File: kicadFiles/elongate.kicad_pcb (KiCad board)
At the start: 2 copper layers, 299.3 x 82.3 mm, 123 parts, among them SW1 SW_PUSH, U1 ATMEGA32U4, X1 XTAL_GND

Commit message: [Update] Finished placing components. Almost done routing. Logos still pending.
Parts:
- removed C1, C2, C3, C4, C5, C6, C7: 22pF, Capacitor_SMD:C_0805_2012Metric_Pad1.15x1.40mm_HandSolder
- removed D_0, D_1, D_2, D_3, D_4, D_5, D_6, D_7, D_8, D_9, D_A, D_ALT, D_ALT1, D_B, D_BS, D_C, D_COMMA, D_CTRL, D_CTRL1, D_D, D_DOT, D_DOWN, D_E, D_ENTER, D_F, D_FN1, D_FN2, D_G, D_H, D_I, D_J, D_K, D_L, D_LEFT, D_M, D_N, D_O, D_P, D_Q, D_R, D_RIGHT, D_S, D_SHIFT, D_SPACE, D_T, D_TAB, D_U, D_UP, D_V, D_W, D_WIN, D_X, D_Y, D_Z: D, keyboard_parts:D_SOD123_axial
- removed K_0, K_1, K_2, K_3, K_4, K_5, K_6, K_7, K_8, K_9, K_A, K_ALT1, K_B, K_BS, K_C, K_COMMA, K_D, K_DOT, K_DOWN, K_E, K_F, K_G, K_H, K_I, K_J, K_K, K_L, K_LEFT, K_M, K_N, K_O, K_P, K_Q, K_R, K_RIGHT, K_S, K_T, K_TAB, K_U, K_UP, K_V, K_W, K_WIN, K_X, K_Y, K_Z: KEYSW, MX_Alps_Hybrid:MX-1U-NoLED
- removed K_ALT, K_CTRL, K_CTRL1, K_FN1: KEYSW, MX_Alps_Hybrid:MX-1.25U-NoLED
- removed K_ENTER, K_SHIFT: KEYSW, MX_Alps_Hybrid:MX-1.75U-NoLED
- removed K_FN2: KEYSW, MX_Alps_Hybrid:MX-2.25U-NoLED
- removed K_SPACE: KEYSW, MX_Alps_Hybrid:MX-2.75U-NoLED
- removed R1, R2: 10k, Resistor_SMD:R_0805_2012Metric_Pad1.15x1.40mm_HandSolder
- removed R3, R4: 22u, Resistor_SMD:R_0805_2012Metric_Pad1.15x1.40mm_HandSolder
- removed U1: ATMEGA32U4, Package_QFP:TQFP-44_10x10mm_P0.8mm
- removed USB1: USB_mini_micro_B, keyboard_parts:USB_miniB_hirose_5S8
- added CB1: 1uF, Capacitor_SMD:C_0805_2012Metric_Pad1.15x1.40mm_HandSolder, F.Cu at (238.0, 23.3)
- added CB2: 100nF, Capacitor_SMD:C_0805_2012Metric_Pad1.15x1.40mm_HandSolder, F.Cu at (238.5, 28.8)
- added CB3: 100nF, Capacitor_SMD:C_0805_2012Metric_Pad1.15x1.40mm_HandSolder, F.Cu at (238.5, 31.0)
- added CB4: 100nF, Capacitor_SMD:C_0805_2012Metric_Pad1.15x1.40mm_HandSolder, F.Cu at (220.5, 31.3)
- added CB5: 100nF, Capacitor_SMD:C_0805_2012Metric_Pad1.15x1.40mm_HandSolder, F.Cu at (238.5, 36.7)
- added CB6: 100nF, Capacitor_SMD:C_0805_2012Metric_Pad1.15x1.40mm_HandSolder, F.Cu at (226.3, 42.5)
- added CF1: 1u, Capacitor_SMD:C_0805_2012Metric_Pad1.15x1.40mm_HandSolder, F.Cu at (246.5, 18.8)
- added CRST1: 100nF, Capacitor_SMD:C_0805_2012Metric_Pad1.15x1.40mm_HandSolder, F.Cu at (220.1, 24.1)
- added CSH1: 100nF, Capacitor_SMD:C_0805_2012Metric_Pad1.15x1.40mm_HandSolder, F.Cu at (228.7, 9.12)
- added CU1: 1uF, Capacitor_SMD:C_0805_2012Metric_Pad1.15x1.40mm_HandSolder, F.Cu at (229.5, 24.0)
- added CUSB1: 100nF, Capacitor_SMD:C_0805_2012Metric_Pad1.15x1.40mm_HandSolder, F.Cu at (238.3, 11.3)
- added CX1: 8.2pF, Capacitor_SMD:C_0805_2012Metric_Pad1.15x1.40mm_HandSolder, F.Cu at (214.8, 31.5)
- added CX2: 8.2pF, Capacitor_SMD:C_0805_2012Metric_Pad1.15x1.40mm_HandSolder, F.Cu at (215.0, 41.3)
- added D1: 1N4148, acheron_Components:D_THT_7.62mm_SOD-123, F.Cu at (19.1, 9.53)
- added D10: 1N4148, acheron_Components:D_THT_7.62mm_SOD-123, F.Cu at (190.5, 9.53)
- added D11: 1N4148, acheron_Components:D_THT_7.62mm_SOD-123, F.Cu at (208.2, 9.53)
- added D12: 1N4148, acheron_Components:D_THT_7.62mm_SOD-123, F.Cu at (210.9, 9.53)
- added D13: 1N4148, acheron_Components:D_THT_7.62mm_SOD-123, F.Cu at (257.2, 9.53)
- added D14: 1N4148, acheron_Components:D_THT_7.62mm_SOD-123, F.Cu at (276.2, 9.53)
- added D15: 1N4148, acheron_Components:D_THT_7.62mm_SOD-123, F.Cu at (285.8, 17.7)
- added D16: 1N4148, acheron_Components:D_THT_7.62mm_SOD-123, F.Cu at (21.4, 28.6)
- added D17: 1N4148, acheron_Components:D_THT_7.62mm_SOD-123, F.Cu at (42.9, 28.6)
- added D18: 1N4148, acheron_Components:D_THT_7.62mm_SOD-123, F.Cu at (61.9, 28.6)
- added D19: 1N4148, acheron_Components:D_THT_7.62mm_SOD-123, F.Cu at (81.0, 28.6)
- added D2: 1N4148, acheron_Components:D_THT_7.62mm_SOD-123, F.Cu at (38.1, 9.53)
- added D20: 1N4148, acheron_Components:D_THT_7.62mm_SOD-123, F.Cu at (100.0, 28.6)
- added D21: 1N4148, acheron_Components:D_THT_7.62mm_SOD-123, F.Cu at (119.1, 28.6)
- added D22: 1N4148, acheron_Components:D_THT_7.62mm_SOD-123, F.Cu at (138.1, 28.6)
- added D23: 1N4148, acheron_Components:D_THT_7.62mm_SOD-123, F.Cu at (157.2, 28.6)
- added D24: 1N4148, acheron_Components:D_THT_7.62mm_SOD-123, F.Cu at (176.2, 28.6)
- added D25: 1N4148, acheron_Components:D_THT_7.62mm_SOD-123, F.Cu at (195.3, 28.6)
- added D26: 1N4148, acheron_Components:D_THT_7.62mm_SOD-123, F.Cu at (202.4, 28.6)
- added D27: 1N4148, acheron_Components:D_THT_7.62mm_SOD-123, F.Cu at (257.2, 28.6)
- added D28: 1N4148, acheron_Components:D_THT_7.62mm_SOD-123, F.Cu at (276.2, 28.6)
- added D29: 1N4148, acheron_Components:D_THT_7.62mm_SOD-123, F.Cu at (285.8, 20.3)
- added D3: 1N4148, acheron_Components:D_THT_7.62mm_SOD-123, F.Cu at (57.1, 9.53)
- added D30: 1N4148, acheron_Components:D_THT_7.62mm_SOD-123, F.Cu at (28.6, 47.6)
- added D31: 1N4148, acheron_Components:D_THT_7.62mm_SOD-123, F.Cu at (52.4, 47.6)
- added D32: 1N4148, acheron_Components:D_THT_7.62mm_SOD-123, F.Cu at (71.4, 47.6)
- added D33: 1N4148, acheron_Components:D_THT_7.62mm_SOD-123, F.Cu at (90.5, 47.6)
- added D34: 1N4148, acheron_Components:D_THT_7.62mm_SOD-123, F.Cu at (109.5, 47.6)
- added D35: 1N4148, acheron_Components:D_THT_7.62mm_SOD-123, F.Cu at (128.6, 47.6)
- added D36: 1N4148, acheron_Components:D_THT_7.62mm_SOD-123, F.Cu at (147.6, 47.6)
- added D37: 1N4148, acheron_Components:D_THT_7.62mm_SOD-123, F.Cu at (166.7, 47.6)
- added D38: 1N4148, acheron_Components:D_THT_7.62mm_SOD-123, F.Cu at (185.7, 47.6)
- added D39: 1N4148, acheron_Components:D_THT_7.62mm_SOD-123, F.Cu at (209.6, 47.6)
- added D4: 1N4148, acheron_Components:D_THT_7.62mm_SOD-123, F.Cu at (76.2, 9.53)
- added D40: 1N4148, acheron_Components:D_THT_7.62mm_SOD-123, F.Cu at (235.7, 52.4)
- added D41: 1N4148, acheron_Components:D_THT_7.62mm_SOD-123, F.Cu at (257.2, 47.6)
- added D42: 1N4148, acheron_Components:D_THT_7.62mm_SOD-123, F.Cu at (276.2, 47.6)
- added D43: 1N4148, acheron_Components:D_THT_7.62mm_SOD-123, F.Cu at (285.8, 38.1)
- added D44: 1N4148, acheron_Components:D_THT_7.62mm_SOD-123, F.Cu at (21.4, 66.7)
- added D45: 1N4148, acheron_Components:D_THT_7.62mm_SOD-123, F.Cu at (42.9, 66.7)
- added D46: 1N4148, acheron_Components:D_THT_7.62mm_SOD-123, F.Cu at (64.3, 66.7)
- added D47: 1N4148, acheron_Components:D_THT_7.62mm_SOD-123, F.Cu at (107.2, 66.7)
- added D48: 1N4148, acheron_Components:D_THT_7.62mm_SOD-123, F.Cu at (164.3, 66.7)
- added D49: 1N4148, acheron_Components:D_THT_7.62mm_SOD-123, F.Cu at (190.5, 66.7)
- added D5: 1N4148, acheron_Components:D_THT_7.62mm_SOD-123, F.Cu at (95.2, 9.53)
- added D50: 1N4148, acheron_Components:D_THT_7.62mm_SOD-123, F.Cu at (214.3, 71.4)
- added D51: 1N4148, acheron_Components:D_THT_7.62mm_SOD-123, F.Cu at (233.4, 71.4)
- added D52: 1N4148, acheron_Components:D_THT_7.62mm_SOD-123, F.Cu at (252.4, 71.4)
- added D53: 1N4148, acheron_Components:D_THT_7.62mm_SOD-123, F.Cu at (276.2, 66.7)
- added D54: 1N4148, acheron_Components:D_THT_7.62mm_SOD-123, F.Cu at (285.8, 57.1)
- added D6: 1N4148, acheron_Components:D_THT_7.62mm_SOD-123, F.Cu at (114.3, 9.53)
- added D7: 1N4148, acheron_Components:D_THT_7.62mm_SOD-123, F.Cu at (133.3, 9.53)
- added D8: 1N4148, acheron_Components:D_THT_7.62mm_SOD-123, F.Cu at (152.4, 9.53)
- added D9: 1N4148, acheron_Components:D_THT_7.62mm_SOD-123, F.Cu at (171.4, 9.53)
- added DF1: RB060M-60TR, acheron_Components:D_SOD-123, F.Cu at (249.1, 18.7)
- added F1: Polyfuse, Fuse:Fuse_1812_4532Metric_Pad1.30x3.40mm_HandSolder, F.Cu at (238.9, 17.9)
- added J1: USB_B_Mini, acheron_Connectors:USB_MiniB_Hirose_UX60-MB-5S8, F.Cu at (233.5, 7.53)
- added RDM1: 22, Resistor_SMD:R_0805_2012Metric_Pad1.15x1.40mm_HandSolder, F.Cu at (234.0, 19.8)
- added RDP1: 22, Resistor_SMD:R_0805_2012Metric_Pad1.15x1.40mm_HandSolder, F.Cu at (232.0, 19.8)
- added RF1: 10k, Resistor_SMD:R_0805_2012Metric_Pad1.15x1.40mm_HandSolder, F.Cu at (243.8, 18.8)
- added RHWB1: 1k, Resistor_SMD:R_0805_2012Metric_Pad1.15x1.40mm_HandSolder, F.Cu at (236.0, 41.5)
- added RRST1: 4.7k, Resistor_SMD:R_0805_2012Metric_Pad1.15x1.40mm_HandSolder, F.Cu at (220.1, 26.1)
- added RRST2: 330R, Resistor_SMD:R_0805_2012Metric_Pad1.15x1.40mm_HandSolder, F.Cu at (220.1, 22.1)
- added RSH1: 1M, Resistor_SMD:R_0805_2012Metric_Pad1.15x1.40mm_HandSolder, F.Cu at (226.5, 9.12)
- added SW10: MXSwitch, acheron_MXA:MXA100, F.Cu at (181.0, 9.53)
- added SW11: MXSwitch, acheron_MXA:MXA100, F.Cu at (200.0, 9.53)
- added SW12: MXSwitch, acheron_MXA:MXA100, F.Cu at (219.1, 9.53)
- added SW13: MXSwitch, acheron_MXA:MXA100, F.Cu at (247.7, 9.53)
- added SW14: MXSwitch, acheron_MXA:MXA100, F.Cu at (266.7, 9.53)
- added SW15: MXSwitch, acheron_MXA:MXA100, F.Cu at (285.8, 9.53)
- added SW16: MXSwitch, acheron_MXA:MXA125, F.Cu at (11.9, 28.6)
- added SW17: MXSwitch, acheron_MXA:MXA100, F.Cu at (33.3, 28.6)
- added SW18: MXSwitch, acheron_MXA:MXA100, F.Cu at (52.4, 28.6)
- added SW19: MXSwitch, acheron_MXA:MXA100, F.Cu at (71.4, 28.6)
- added SW2: MXSwitch, acheron_MXA:MXA100, F.Cu at (28.6, 9.53)
- added SW20: MXSwitch, acheron_MXA:MXA100, F.Cu at (90.5, 28.6)
- added SW21: MXSwitch, acheron_MXA:MXA100, F.Cu at (109.5, 28.6)
- added SW22: MXSwitch, acheron_MXA:MXA100, F.Cu at (128.6, 28.6)
- added SW23: MXSwitch, acheron_MXA:MXA100, F.Cu at (147.6, 28.6)
- added SW24: MXSwitch, acheron_MXA:MXA100, F.Cu at (166.7, 28.6)
- added SW25: MXSwitch, acheron_MXA:MXA100, F.Cu at (185.7, 28.6)
- added SW26: MXSwitch, acheron_MXA:MXA175, F.Cu at (211.9, 28.6)
- added SW27: MXSwitch, acheron_MXA:MXA100, F.Cu at (247.7, 28.6)
- added SW28: MXSwitch, acheron_MXA:MXA100, F.Cu at (266.7, 28.6)
- added SW29: MXSwitch, acheron_MXA:MXA100, F.Cu at (285.8, 28.6)
- added SW3: MXSwitch, acheron_MXA:MXA100, F.Cu at (47.6, 9.53)
- added SW30: MXSwitch, acheron_MXA:MXA175, F.Cu at (16.7, 47.6)
- added SW31: MXSwitch, acheron_MXA:MXA100, F.Cu at (42.9, 47.6)
- added SW32: MXSwitch, acheron_MXA:MXA100, F.Cu at (61.9, 47.6)
- added SW33: MXSwitch, acheron_MXA:MXA100, F.Cu at (81.0, 47.6)
- added SW34: MXSwitch, acheron_MXA:MXA100, F.Cu at (100.0, 47.6)
- added SW35: MXSwitch, acheron_MXA:MXA100, F.Cu at (119.1, 47.6)
- added SW36: MXSwitch, acheron_MXA:MXA100, F.Cu at (138.1, 47.6)
- added SW37: MXSwitch, acheron_MXA:MXA100, F.Cu at (157.2, 47.6)
- added SW38: MXSwitch, acheron_MXA:MXA100, F.Cu at (176.2, 47.6)
- added SW39: MXSwitch, acheron_MXA:MXA125, F.Cu at (197.6, 47.6)
- added SW4: MXSwitch, acheron_MXA:MXA100, F.Cu at (66.7, 9.53)
- added SW40: MXSwitch, acheron_MXA:MXA100, F.Cu at (223.8, 52.4)
- added SW41: MXSwitch, acheron_MXA:MXA100, F.Cu at (247.7, 47.6)
- added SW42: MXSwitch, acheron_MXA:MXA100, F.Cu at (266.7, 47.6)
- added SW43: MXSwitch, acheron_MXA:MXA100, F.Cu at (285.8, 47.6)
- added SW44: MXSwitch, acheron_MXA:MXA125, F.Cu at (11.9, 66.7)
- added SW45: MXSwitch, acheron_MXA:MXA100, F.Cu at (33.3, 66.7)
- added SW46: MXSwitch, acheron_MXA:MXA125, F.Cu at (54.8, 66.7)
- added SW47: MXSwitch, acheron_MXA:MXA225R, F.Cu at (88.1, 66.7)
- added SW48: MXSwitch, acheron_MXA:MXA275R, F.Cu at (145.3, 66.7)
- added SW49: MXSwitch, acheron_MXA:MXA100, F.Cu at (181.0, 66.7)
- added SW5: MXSwitch, acheron_MXA:MXA100, F.Cu at (85.7, 9.53)
- added SW50: MXSwitch, acheron_MXA:MXA100, F.Cu at (204.8, 71.4)
- added SW51: MXSwitch, acheron_MXA:MXA100, F.Cu at (223.8, 71.4)
- added SW52: MXSwitch, acheron_MXA:MXA100, F.Cu at (242.9, 71.4)
- added SW53: MXSwitch, acheron_MXA:MXA100, F.Cu at (266.7, 66.7)
- added SW54: MXSwitch, acheron_MXA:MXA100, F.Cu at (285.8, 66.7)
- added SW6: MXSwitch, acheron_MXA:MXA100, F.Cu at (104.8, 9.53)
- added SW7: MXSwitch, acheron_MXA:MXA100, F.Cu at (123.8, 9.53)
- added SW8: MXSwitch, acheron_MXA:MXA100, F.Cu at (142.9, 9.53)
- added SW9: MXSwitch, acheron_MXA:MXA100, F.Cu at (161.9, 9.53)
- added SW_RST1: SW_Push, acheron_Hardware:smdPushBtn, F.Cu at (216.8, 17.8)
- added U2: USBLC6-2SC6, acheron_Components:SOT-23-6, F.Cu at (234.0, 12.0)
- added U3: ATMEGA32U4, acheron_Components:TQPF-44_10x10mm_P0.8mm, F.Cu at (229.5, 33.5)
- SW1: value SW_PUSH -> MXSwitch; footprint Button_Switch_SMD:SW_SPST_TL3342 -> acheron_MXA:MXA100; moved to F.Cu
- X1: value XTAL_GND -> 16MHz; footprint Crystal:Crystal_SMD_5032-4Pin_5.0x3.2mm -> acheron_Components:Crystal_SMD_5032-4Pin-HandSolder; moved to F.Cu
- moved SW1 247.4 mm to (9.53, 9.53)
- moved X1 102.4 mm to (215.0, 36.3), turned to 90 degrees
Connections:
- SW1 pad 1: GND -> Col1
- X1 pad 1: Net-(C1-Pad1) -> /XTAL1
- X1 pad 2: Net-(C2-Pad1) -> GND
- X1 pad 3: GND -> /XTAL2
- X1 pad 4: Net-(X1-Pad4) -> GND
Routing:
- net /row0: track 331.7 -> 0.00 mm, vias 2 -> 0
- net Row2: track 0.00 -> 321.8 mm
- net Row4: track 0.00 -> 302.2 mm
- net /row1: track 299.3 -> 0.00 mm, vias 1 -> 0
- net Row1: track 0.00 -> 296.1 mm
- net Row3: track 0.00 -> 295.3 mm
- net /row3: track 290.8 -> 0.00 mm, vias 1 -> 0
- net /row2: track 277.2 -> 0.00 mm, vias 1 -> 0
- net VCC: track 265.0 -> 0.00 mm, vias 4 -> 0
- net /col12: track 191.9 -> 0.00 mm, vias 1 -> 0
- net Net-(R3-Pad1): track 185.6 -> 0.00 mm
- net /col0: track 184.6 -> 0.00 mm
- net /col11: track 178.1 -> 0.00 mm, vias 1 -> 0
- net Net-(C3-Pad1): track 176.8 -> 0.00 mm
- net Net-(R4-Pad1): track 176.3 -> 0.00 mm
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- added copper zone on B.Cu, net /SHIELD
- added copper zone on F.Cu, net GND
- removed copper zone on F.Cu, net VCC
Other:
- board size 299.3 x 82.3 mm -> 294 x 82 mm
- net class Default: clearance 0.2 -> 0.13
- net class Super Thick added: clearance 0.5, trace_width 1, via_dia 0.8, via_drill 0.4
- net class Thick added: clearance 0.25, trace_width 0.5, via_dia 0.8, via_drill 0.4
- rule trace_clearance: 0.2 -> 0.13
- board text added: "ATMEGA32U4"

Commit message: [Update] Finished routing
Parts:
- moved RHWB1 147.2 mm to (373.5, 94.0)
- moved CB5 145.7 mm to (373.5, 91.5)
- moved CSH1 144.8 mm to (362.7, 64.1)
- moved RSH1 144.8 mm to (360.5, 64.1)
- moved D11 144.5 mm to (342.2, 63.5)
- moved D23 144.5 mm to (291.2, 82.6)
- moved D52 144.5 mm to (386.4, 125.4)
- moved D7 144.5 mm to (267.4, 63.5)
- moved SW10 144.5 mm to (315.0, 63.5)
- moved SW37 144.5 mm to (291.2, 101.6)
- moved SW48 144.5 mm to (279.3, 120.7)
- moved SW49 144.5 mm to (315.0, 120.7)
- moved SW50 144.5 mm to (338.8, 125.4)
- moved CRST1 144.5 mm to (354.1, 78.1)
- moved CUSB1 144.5 mm to (372.3, 65.3)
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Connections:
- U3 pad 12: Net-(U3-Pad12) -> Col4
- U3 pad 19: Net-(U3-Pad19) -> Col6
- U3 pad 20: Net-(U3-Pad20) -> Col7
- U3 pad 21: Net-(U3-Pad21) -> Col9
- U3 pad 22: Net-(U3-Pad22) -> Col12
- U3 pad 25: Net-(U3-Pad25) -> Col1
- U3 pad 26: Net-(U3-Pad26) -> Col2
- U3 pad 27: Net-(U3-Pad27) -> Col3
- U3 pad 28: Net-(U3-Pad28) -> Col5
- U3 pad 29: Net-(U3-Pad29) -> Col8
- U3 pad 30: Net-(U3-Pad30) -> Col10
- U3 pad 31: Net-(U3-Pad31) -> Col11
- U3 pad 32: Net-(U3-Pad32) -> Col13
- U3 pad 36: Net-(U3-Pad36) -> Row4
- U3 pad 37: Net-(U3-Pad37) -> Row3
- U3 pad 38: Net-(U3-Pad38) -> Col14
- U3 pad 39: Net-(U3-Pad39) -> Col15
- U3 pad 40: Net-(U3-Pad40) -> Row2
- U3 pad 41: Net-(U3-Pad41) -> Row1
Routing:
- net Col1: track 84.7 -> 347.0 mm
- net Col2: track 58.8 -> 298.5 mm
- net Col3: track 69.8 -> 291.4 mm
- net Col5: track 65.4 -> 252.1 mm
- net Col4: track 42.8 -> 215.4 mm
- net Col6: track 42.8 -> 184.3 mm
- net Col8: track 65.8 -> 197.8 mm
- net Col7: track 42.8 -> 164.9 mm
- net Col10: track 64.3 -> 158.9 mm
- net Col9: track 42.8 -> 126.7 mm
- net Col11: track 68.7 -> 139.3 mm
- net Row4: track 302.2 -> 356.0 mm
- net Col15: track 64.3 -> 116.3 mm
- net Row1: track 296.1 -> 340.7 mm
- net Row3: track 295.3 -> 334.9 mm
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
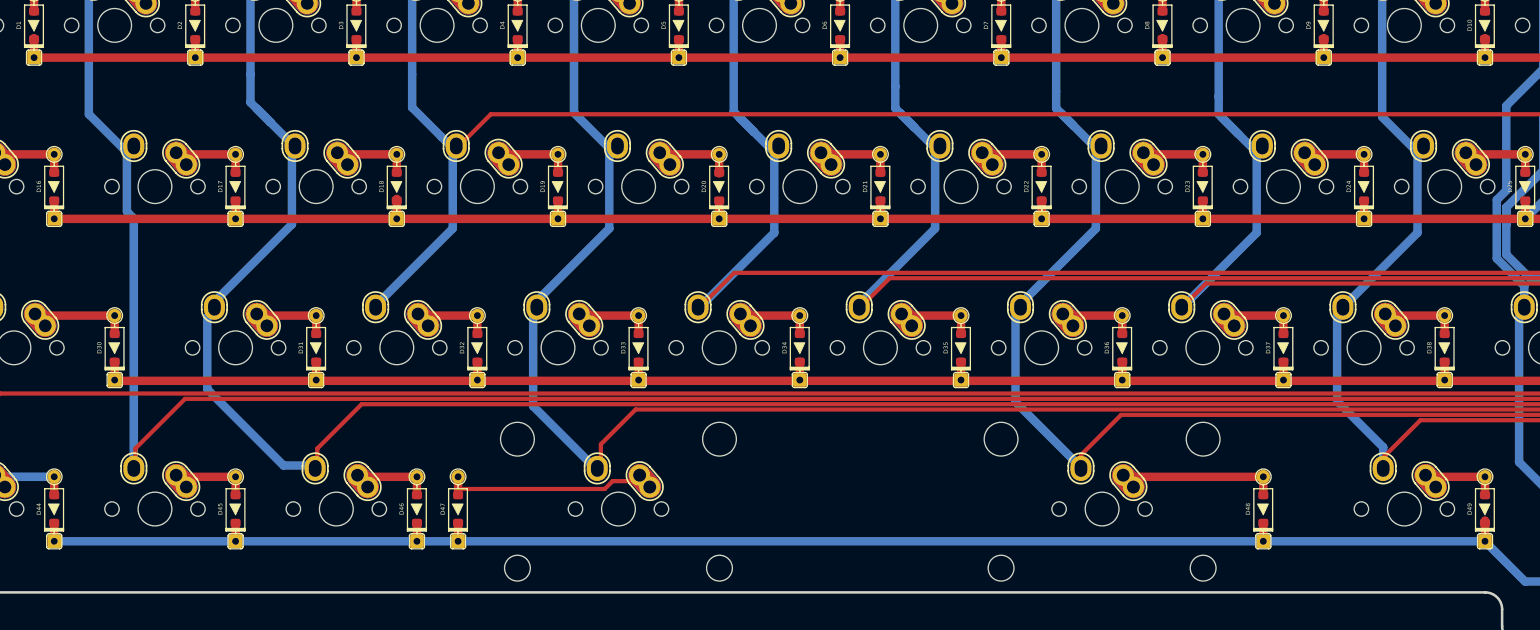
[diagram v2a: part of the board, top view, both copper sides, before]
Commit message: [Update] Added logos and label
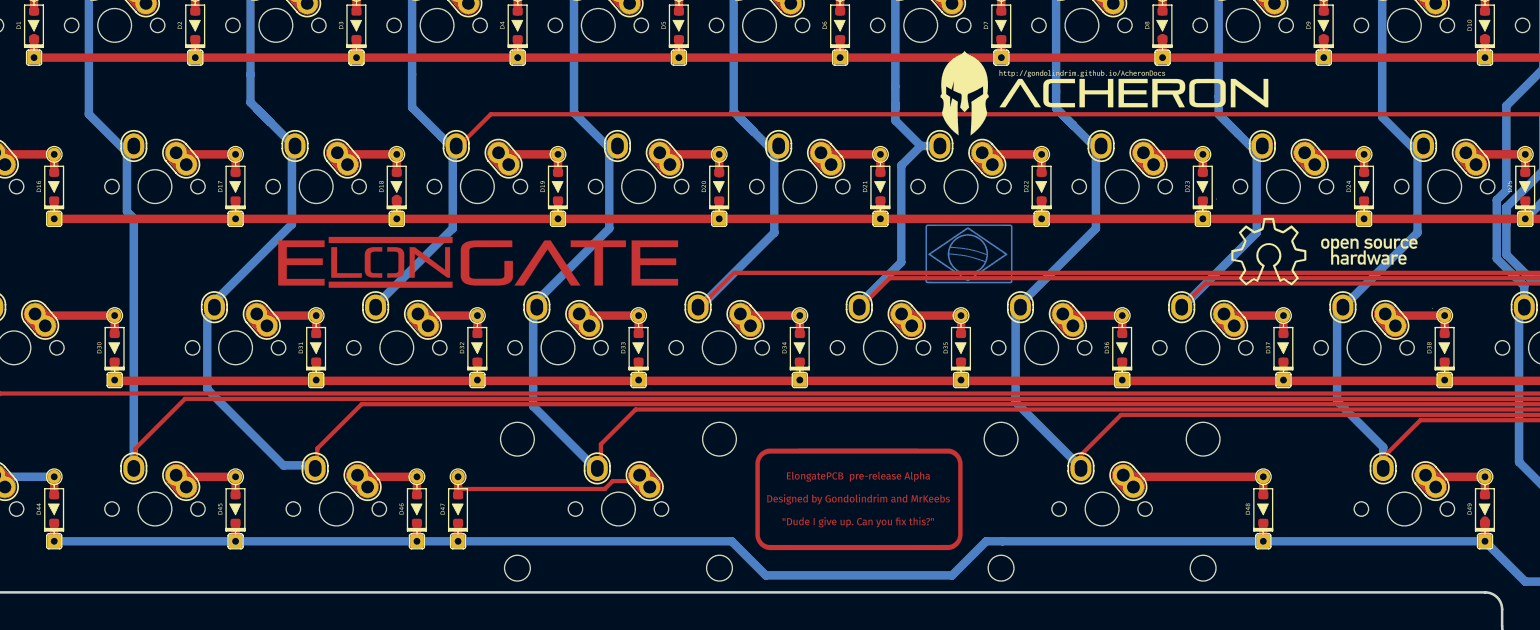
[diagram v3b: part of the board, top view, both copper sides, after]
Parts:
- added L1: AcheronLogo, acheron_Logos:acheronLong, F.Cu at (279.5, 71.5)
- added L2: ElongateLogoPlated, elongateGraphics:elongateLogo, F.Cu at (205.5, 91.5)
- added L3: ElongateLabel, elongateGraphics:elongateLabel, F.Cu at (250.5, 119.5)
- added L4: ElongateLabelMask, elongateGraphics:elongateLabelMask, F.Cu at (250.5, 119.5)
- added L5: OSHLogo, oshLogo:osh-logo, F.Cu at (305.5, 90.5)
- added L6: BRFlag, oshLogo:brazilFlag, F.Cu at (263.5, 90.5)
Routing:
- net Row4: track 356.0 -> 359.3 mm
- net Col7: track 164.9 -> 163.8 mm
